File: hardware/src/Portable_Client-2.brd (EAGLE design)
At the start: 48.9 x 36.8 mm, 24 parts, among them IC3 MC78M05ABT, U1 ATMEGA328P-AU, Y1 12MHZ

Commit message: New client board V0.1
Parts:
- added C4, C5, C6: (no value), adafruit:C0402
- added DBG1: (no value), SparkFun-Connectors:1X02
- added R5, R6, R7, R8: 330, adafruit:R0603
- added R9: 4.7k, adafruit:R0603
- added RESET: SWITCH-MOMENTARY-2SMD-1101NE, SparkFun-Electromechanical:TACTILE-SWITCH-1101NE
- moved POW 0.95 mm to (45.7, 12.4)
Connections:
- new net MISO: LCD/TOUCH.2, LCD/TOUCH.9, NFC.5, R5.2
- new net MOSI: LCD/TOUCH.3, LCD/TOUCH.6, NFC.6, R6.2
- new net N$3: R8.2, RESET.2
- new net SCK: LCD/TOUCH.5, LCD/TOUCH.8, NFC.7, R7.2
- net 3V3: now also C4.1, C5.1, DBG1.2, R9.1
- net D11: now also R6.1; no longer LCD/TOUCH.3, LCD/TOUCH.6, NFC.6
- net D12: now also R5.1; no longer LCD/TOUCH.2, LCD/TOUCH.9, NFC.5
- net D13: now also R7.1; no longer LCD/TOUCH.5, LCD/TOUCH.8, NFC.7
- net GND: now also C4.2, C5.2, C6.2, R8.1
- net RESET: now also C6.1, R9.2, RESET.1
- net VIN: now also DBG1.1
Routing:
- net MISO: track 0.00 -> 27.1 mm, vias 0 -> 1
- net MOSI: track 0.00 -> 18.2 mm
- net SCK: track 0.00 -> 17.6 mm
- net D13: track 52.5 -> 36.7 mm
- net 3V3: track 145.2 -> 159.9 mm, vias 5 -> 6
- net RESET: track 34.4 -> 47.5 mm, vias 1 -> 2
- net D11: track 51.0 -> 42.9 mm, vias 1 -> 4
- net D12: track 59.5 -> 66.7 mm, vias 0 -> 1
- net VIN: track 9.03 -> 15.9 mm, vias 0 -> 1
- net N$3: track 0.00 -> 5.82 mm
- net GND: track 178.3 -> 182.7 mm, vias 4 -> 5
- net D4: track 33.5 -> 32.6 mm
- net D19: track 29.3 -> 29.9 mm
- added copper zone on layer 1, net GND
- added copper zone on layer 16, net GND
- added copper zone on layer 16, net N$8

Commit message: fix a few board errors     -MOSI and MISO swapped on LCD and SPI headers     -change esp8266 capacitor to surface mount
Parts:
- C3: value (none) -> 100uf; device SparkFun-Capacitors:CPOL-RADIAL-10UF-25V -> rcl:153CLV-0605
- C4, C5, C6: value (none) -> .1uf
- moved R3 7.13 mm to (5.08, 20.3)
- moved R4 6.55 mm to (3.17, 20.3)
- moved C3 2.56 mm to (13.3, 17.8)
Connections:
- net 3V3: now also C3.+; no longer C3.1
- net D11: now also ICSP.4; no longer ICSP.1
- net D12: now also ICSP.1; no longer ICSP.4
- net GND: now also C3.-; no longer C3.2
- net MISO: now also LCD/TOUCH.6; no longer LCD/TOUCH.9
- net MOSI: now also LCD/TOUCH.9; no longer LCD/TOUCH.6
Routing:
- net D12: track 66.7 -> 74.4 mm
- net MOSI: track 18.2 -> 24.4 mm, vias 0 -> 1
- net N$7: track 6.06 -> 12.3 mm
- net N$6: track 17.5 -> 23.6 mm
- net MISO: track 27.1 -> 24.5 mm
- net D11: track 42.9 -> 45.4 mm
- net 3V3: track 159.9 -> 158.2 mm, vias 6 -> 7
- net GND: track 182.7 -> 183.4 mm, vias 5 -> 6

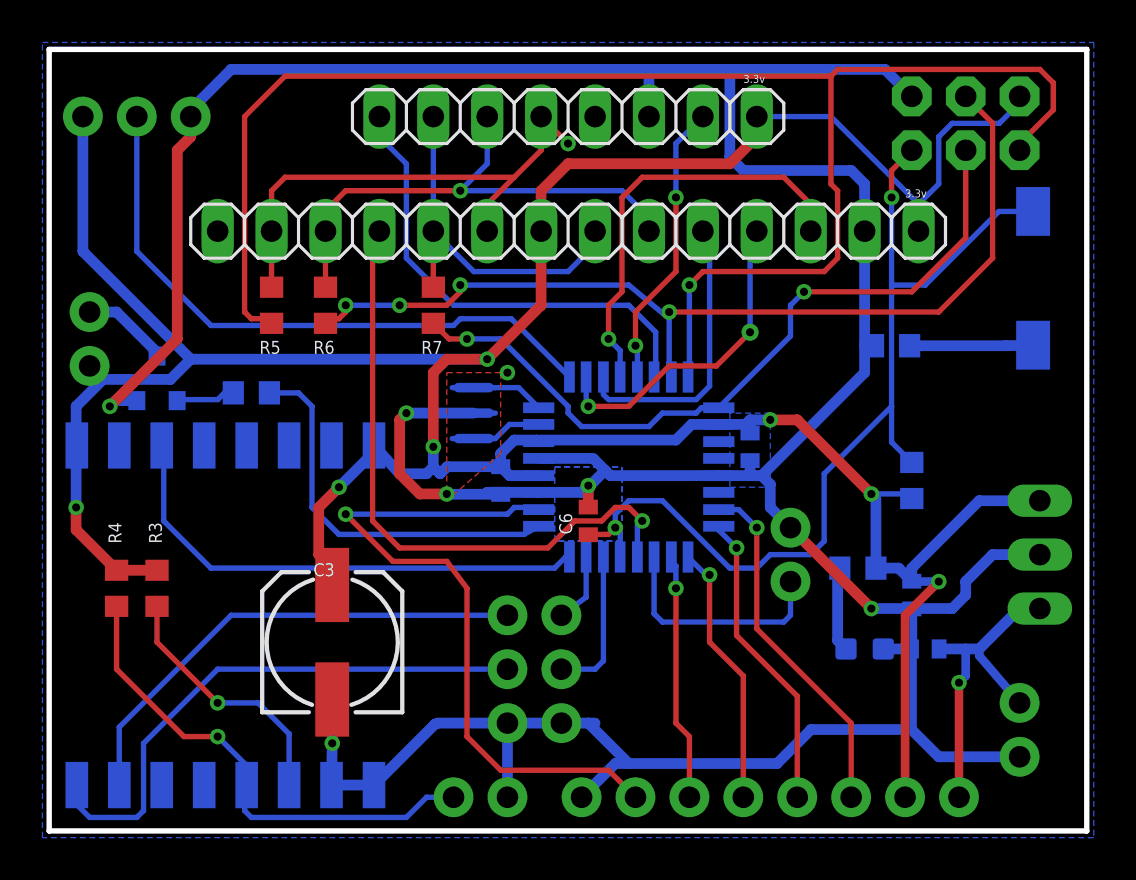
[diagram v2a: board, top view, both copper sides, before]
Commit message: Fix DRC errors in wifi client board.
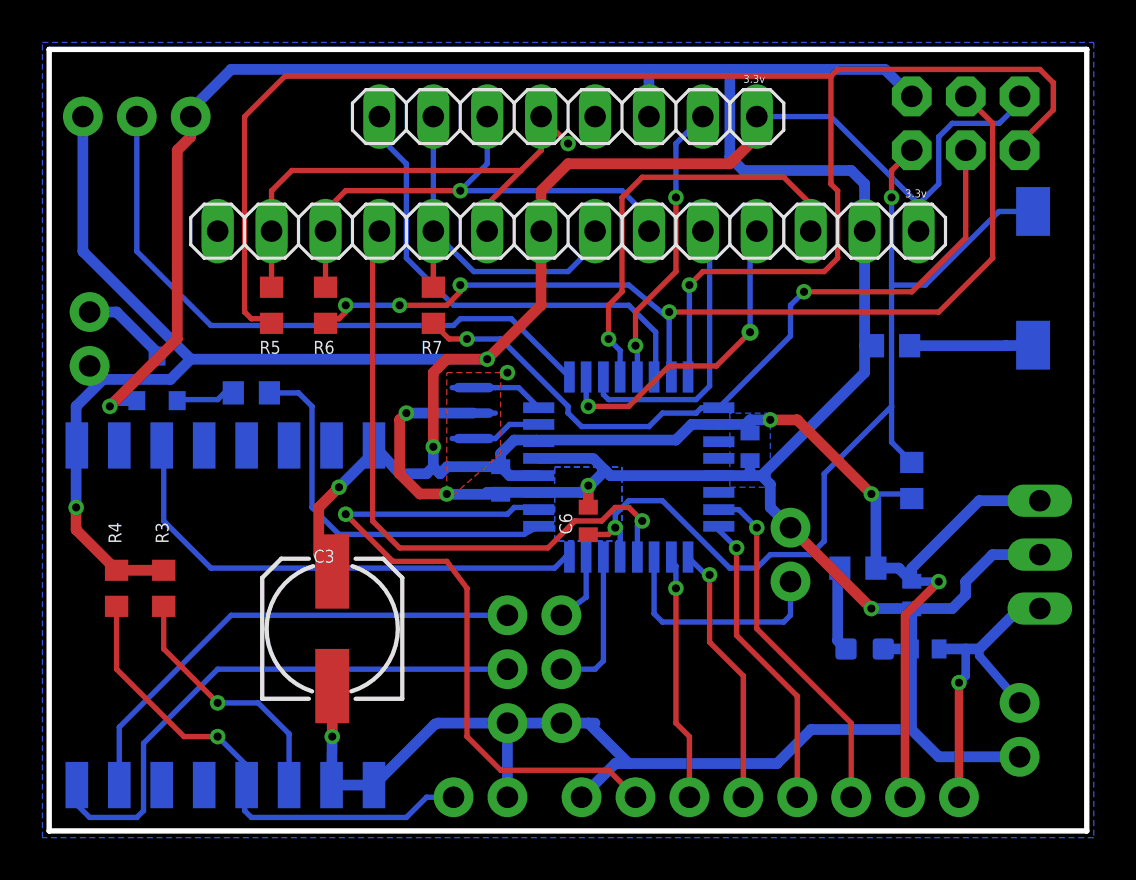
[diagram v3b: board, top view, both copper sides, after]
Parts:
- moved C3 0.63 mm to (13.3, 18.4)
- moved R3 0.32 mm to (5.40, 20.3)
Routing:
- net GND: track 183.4 -> 184.0 mm
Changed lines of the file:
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@@
 <attribute name="NAME" x="8.9535" y="30.861" size="0.6096" layer="26" rot="MR180"/>
 </element>
-<element name="R3" library="adafruit" package="R0603" value="3.3k" x="5.08" y="20.32" smashed="yes" rot="R270">
-<attribute name="NAME" x="4.699" y="23.4315" size="0.6096" layer="25" rot="R270"/>
+<element name="R3" library="adafruit" package="R0603" value="3.3k" x="5.3975" y="20.32" smashed="yes" rot="R270">
+<attribute name="NAME" x="5.0165" y="23.4315" size="0.6096" layer="25" rot="R270"/>
 </element>
 <element name="R4" library="adafruit" package="R0603" value="3.3k" x="3.175" y="20.32" smashed="yes" rot="R270">
@@
 <attribute name="VALUE" x="23.8125" y="13.6525" size="1.27" layer="28" rot="MR180"/>
 </element>
-<element name="C3" library="rcl" package="153CLV-0605" value="100uf" x="13.335" y="17.78" smashed="yes" rot="R90">
-<attribute name="NAME" x="12.446" y="20.8915" size="0.6096" layer="25"/>
-<attribute name="VALUE" x="17.018" y="15.875" size="0.8128" layer="27" rot="R90"/>
+<element name="C3" library="rcl" package="153CLV-0605" value="100uf" x="13.335" y="18.415" smashed="yes" rot="R90">
+<attribute name="NAME" x="12.446" y="21.5265" size="0.6096" layer="25"/>
+<attribute name="VALUE" x="17.018" y="16.51" size="0.8128" layer="27" rot="R90"/>
 </element>
 <element name="C4" library="adafruit" package="C0402" value=".1uf" x="21.2725" y="25.4" smashed="yes" rot="MR270">
@@
 <wire x1="15.22810625" y1="26.65810625" x2="15.3025" y2="26.837709375" width="0.508" layer="16" curve="44.999295"/>
 <wire x1="15.3025" y1="26.837709375" x2="15.3025" y2="27.05" width="0.508" layer="16"/>
-<wire x1="3.175" y1="21.17" x2="5.08" y2="21.17" width="0.508" layer="1"/>
+<wire x1="3.175" y1="21.17" x2="5.3975" y2="21.17" width="0.508" layer="1"/>
 <contactref element="NEOPIXEL" pad="1"/>
 <wire x1="1.5875" y1="36.195" x2="1.5875" y2="42.545" width="0.508" layer="16"/>
@@
 <wire x1="13.6525" y1="25.0825" x2="12.7" y2="24.13" width="0.508" layer="1"/>
 <wire x1="12.7" y1="24.13" x2="12.7" y2="21.9075" width="0.508" layer="1"/>
-<wire x1="12.7" y1="21.9075" x2="13.335" y2="21.2725" width="0.508" layer="1"/>
-<wire x1="13.335" y1="21.2725" x2="13.335" y2="20.48" width="0.508" layer="1"/>
+<wire x1="12.7" y1="21.9075" x2="13.335" y2="21.115" width="0.508" layer="1"/>
 </signal>
 <signal name="N$12">
@@
 <vertex x="23.8125" y="22.5425"/>
 </polygon>
-<wire x1="13.335" y1="15.08" x2="13.335" y2="13.0175" width="0.508" layer="1"/>
-<via x="13.335" y="13.0175" extent="1-16" drill="0.381" shape="octagon"/>
-<wire x1="13.335" y1="13.0175" x2="13.3025" y2="11.05" width="0.508" layer="16"/>
+<wire x1="13.335" y1="15.715" x2="13.335" y2="13.335" width="0.508" layer="1"/>
+<via x="13.335" y="13.335" extent="1-16" drill="0.381" shape="octagon"/>
+<wire x1="13.335" y1="13.335" x2="13.3025" y2="11.05" width="0.508" layer="16"/>
 </signal>
 <signal name="A7">
@@
 <contactref element="R3" pad="2"/>
 <wire x1="11.3025" y1="11.05" x2="11.1125" y2="11.05" width="0.4064" layer="16"/>
-<wire x1="5.08" y1="19.47" x2="5.08" y2="17.78" width="0.254" layer="1"/>
-<wire x1="5.08" y1="17.78" x2="7.9375" y2="14.9225" width="0.254" layer="1"/>
+<wire x1="5.3975" y1="19.47" x2="5.3975" y2="17.4625" width="0.254" layer="1"/>
+<wire x1="5.3975" y1="17.4625" x2="7.9375" y2="14.9225" width="0.254" layer="1"/>
 <via x="7.9375" y="14.9225" extent="1-16" drill="0.381" shape="octagon"/>
 <wire x1="7.9375" y1="14.9225" x2="9.8425" y2="14.9225" width="0.254" layer="16"/>
@@
 <contactref element="NFC" pad="5"/>
 <wire x1="10.4775" y1="37.1475" x2="10.4775" y2="39.0525" width="0.254" layer="1"/>
-<wire x1="10.4775" y1="39.0525" x2="11.1125" y2="39.6875" width="0.254" layer="1"/>
-<wire x1="11.1125" y1="39.6875" x2="21.9075" y2="39.6875" width="0.254" layer="1"/>
-<wire x1="21.9075" y1="39.6875" x2="23.1775" y2="40.9575" width="0.254" layer="1"/>
+<wire x1="10.4775" y1="39.0525" x2="11.43" y2="40.005" width="0.254" layer="1"/>
+<wire x1="11.43" y1="40.005" x2="22.225" y2="40.005" width="0.254" layer="1"/>
+<wire x1="22.225" y1="40.005" x2="23.1775" y2="40.9575" width="0.254" layer="1"/>
 <wire x1="23.1775" y1="40.9575" x2="23.1775" y2="42.545" width="0.254" layer="1"/>
 <wire x1="23.1775" y1="42.545" x2="24.4475" y2="41.275" width="0.254" layer="1"/>
@@
 <wire x1="10.4775" y1="34.505" x2="10.4775" y2="37.1475" width="0.254" layer="1"/>
 <contactref element="LCD/TOUCH" pad="6"/>
-<wire x1="21.9075" y1="39.6875" x2="20.6375" y2="38.4175" width="0.254" layer="1"/>
+<wire x1="22.225" y1="40.005" x2="20.6375" y2="38.4175" width="0.254" layer="1"/>
 <wire x1="20.6375" y1="38.4175" x2="20.6375" y2="37.1475" width="0.254" layer="1"/>
 </signal>
